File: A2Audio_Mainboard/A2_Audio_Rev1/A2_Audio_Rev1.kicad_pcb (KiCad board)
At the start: 4 copper layers, 194 x 109.5 mm, 217 parts, among them IC1 ES9822QPRO, J1 Battery_Connector, J3 BOOT_JUMPER, J4 12401610E4_2A, J5 104031-0811, J6 SFV15R-1STE1HLF, J7 SJ2-35954B-SMT-TR, SW1 SW_Wuerth_450301014042, SW10 EVQ-PUJ02K, SW11 EVQ-PUJ02K, SW4 SW_Wuerth_450301014042, SW8 EVQ-PUJ02K, SW9 EVQ-PUJ02K, U1 USBLC6-2SC6, U10 OPA1622IDRCR, U11 SI4732-A10-GS, U12 OPA1612AIDR, U13 LT3042xMSE, U14 W25Q16JVSS, U15 CM5108000, U16 AP2112K-3.3, U17 AP2112K-1.8, U18 LT6711A, U19 TPS62130, U2 TPS65987DDHRSHR, U20 AP2112K-1.8, U21 TPS61230DRC, U22 AP2112K-1.2, U23 LTC2954ITS8-1_TRPBF, U25 LT3094xDD, U26 TS5A3159DBVR, U27 TPS65131RGE, U3 TUSB546A-DCIRNQR, U4 BQ25895RTWR, U5 MAX17055ETB_T, U6 U_DAC_L, U7 U_DAC_R, U8 TPS7A2018PDBVR, U9 TPS7A2033PDBVR, Y1 Crystal, Y2 27MHz

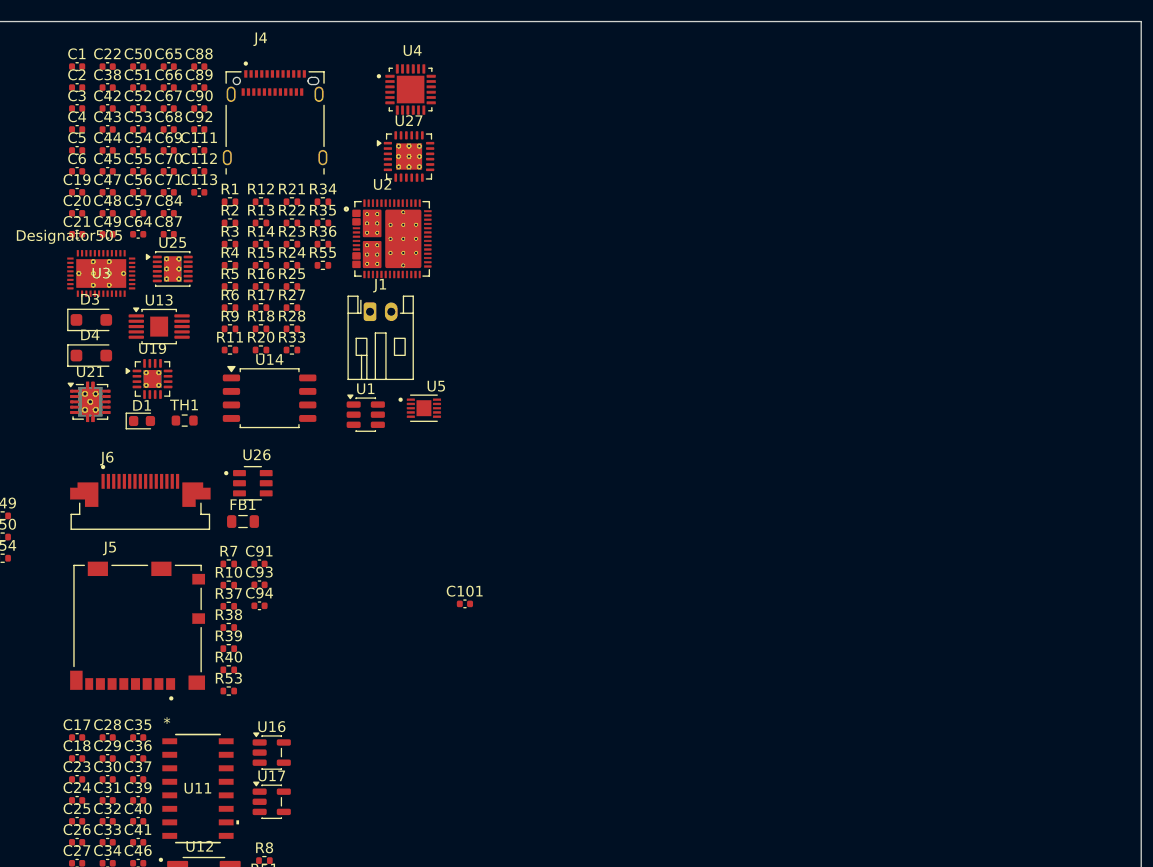
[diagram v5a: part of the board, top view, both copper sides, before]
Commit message: Fixed SD Card logic and power error
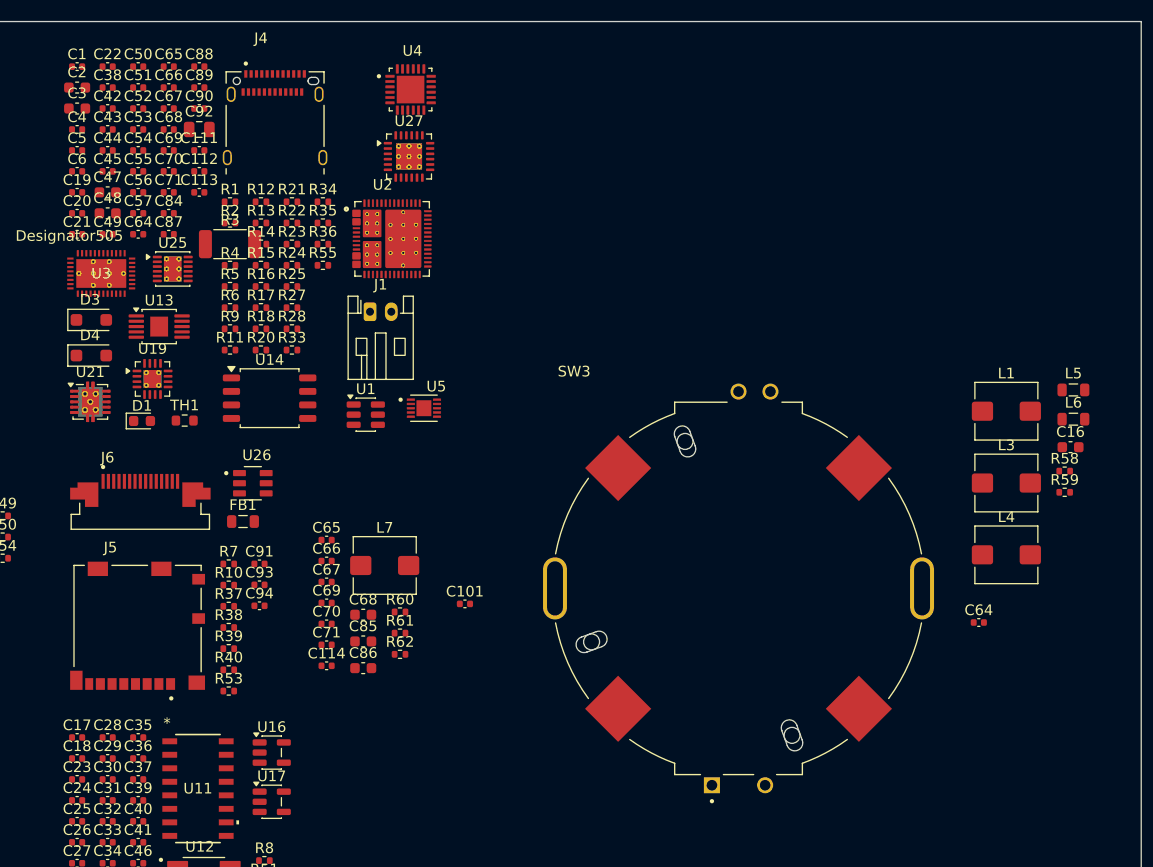
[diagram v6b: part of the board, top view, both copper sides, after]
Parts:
- added C114: 0.1µF, Capacitor_SMD:C_0402_1005Metric, F.Cu at (168.9, 107.3)
- added C16: 10µF, Capacitor_SMD:C_0603_1608Metric, F.Cu at (238.9, 86.8)
- added C64: 10µF, Capacitor_SMD:C_0402_1005Metric, F.Cu at (230.2, 103.2)
- added C65: 0.1µF, Capacitor_SMD:C_0402_1005Metric, F.Cu at (168.9, 95.5)
- added C66: 10µF, Capacitor_SMD:C_0402_1005Metric, F.Cu at (168.9, 97.5)
- added C67: 0.1µF, Capacitor_SMD:C_0402_1005Metric, F.Cu at (168.9, 99.4)
- added C68: 47nF, Capacitor_SMD:C_0603_1608Metric, F.Cu at (172.4, 102.5)
- added C69: 4.7nF, Capacitor_SMD:C_0402_1005Metric, F.Cu at (168.9, 101.4)
- added C70: 220pF, Capacitor_SMD:C_0402_1005Metric, F.Cu at (168.9, 103.4)
- added C71: 1µF, Capacitor_SMD:C_0402_1005Metric, F.Cu at (168.9, 105.3)
- added C85: 22µF, Capacitor_SMD:C_0603_1608Metric, F.Cu at (172.4, 105.0)
- added C86: 22µF, Capacitor_SMD:C_0603_1608Metric, F.Cu at (172.4, 107.5)
- added L1: 1µH, Inductor_SMD:L_Bourns_SRP5030T, F.Cu at (232.8, 83.4)
- added L3: 2.2µH, Inductor_SMD:L_Bourns_SRP5030T, F.Cu at (232.8, 90.1)
- added L4: 1.0µH, Inductor_SMD:L_Bourns_SRP5030T, F.Cu at (232.8, 96.9)
- added L5: 4.7µH, Inductor_SMD:L_0805_2012Metric, F.Cu at (239.1, 81.4)
- added L6: 4.7µH, Inductor_SMD:L_0805_2012Metric, F.Cu at (239.1, 84.1)
- added L7: 1.0µH, Inductor_SMD:L_Bourns_SRP5030T, F.Cu at (174.4, 97.9)
- added R58: 100kΩ, Resistor_SMD:R_0402_1005Metric, F.Cu at (238.3, 89.0)
- added R59: 100kΩ, Resistor_SMD:R_0402_1005Metric, F.Cu at (238.3, 91.0)
- added R60: 120kΩ, Resistor_SMD:R_0402_1005Metric, F.Cu at (175.8, 102.2)
- added R61: 15kΩ, Resistor_SMD:R_0402_1005Metric, F.Cu at (175.8, 104.2)
- added R62: 10kΩ, Resistor_SMD:R_0402_1005Metric, F.Cu at (175.8, 106.2)
- added SW3: RotaryEncoder_Switch, custom:XDCR_RING35-203010-TH, F.Cu at (207.7, 100.0)
- C2, C3, C47, C48: footprint Capacitor_SMD:C_0402_1005Metric -> Capacitor_SMD:C_0603_1608Metric
- C92: value 4.7µF -> 22µF; footprint Capacitor_SMD:C_0402_1005Metric -> Capacitor_SMD:C_0805_2012Metric
- R28: value 23.7kΩ -> 402kΩ
- R3: footprint Resistor_SMD:R_0402_1005Metric -> Resistor_SMD:R_2010_5025Metric
- R34: value 806kΩ -> 1.0MΩ
- R36: value 10kΩ -> 124kΩ
- R4, R5: value 49.9kΩ -> 45.3kΩ
- R9: value R -> 1kΩ
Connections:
- C17 pad 1: /Audio_Engine/-5V_AMP -> EXP
- C23 pad 1: Net-(IC1-AVCC) -> /Recording&Radio_Engine/3v
- C26 pad 1: Net-(IC1-CHIP_EN) -> /Recording&Radio_Engine/3v
- C27 pad 2: Net-(IC1-CHIP_EN) -> /Recording&Radio_Engine/3v
- C28 pad 2: Net-(IC1-AVCC) -> /Recording&Radio_Engine/+5V_AMP
- C29 pad 2: Net-(IC1-AVCC) -> /Recording&Radio_Engine/+5V_AMP
- C30 pad 2: Net-(IC1-AVCC) -> /Recording&Radio_Engine/3v
- C31 pad 2: Net-(IC1-AVCC) -> /Recording&Radio_Engine/+5V_AMP
- C41 pad 1: Net-(IC1-AVCC) -> /Recording&Radio_Engine/3v
- C46 pad 1: Net-(IC1-CHIP_EN) -> Net-(U17-VOUT)
- C80 pad 1: /Power&Battery/DP_AUX_P -> /Power&Battery/DP_AUX_N
- C81 pad 1: /Power&Battery/DP_AUX_N -> /Power&Battery/DP_AUX_P
- C92 pad 2: /Audio_Engine/-5V_AMP -> EXP
- IC1 pad 10: Net-(IC1-AVCC) -> /Recording&Radio_Engine/+5V_AMP
- IC1 pad 21: Net-(IC1-AVCC) -> /Recording&Radio_Engine/+5V_AMP
- IC1 pad 23: Net-(IC1-CHIP_EN) -> /Recording&Radio_Engine/3v
- IC1 pad 29: Net-(IC1-CHIP_EN) -> Net-(IC1-DVDD)
- IC1 pad 30: Net-(IC1-AVCC) -> /Recording&Radio_Engine/3v
- IC1 pad 5: Net-(IC1-AVCC) -> /Recording&Radio_Engine/+5V_AMP
- R21 pad 2: /+3V3_SYS -> CM5_3.3V(OUTPUT)
- R22 pad 2: /+3V3_SYS -> CM5_3.3V(OUTPUT)
- R25 pad 2: /+3V3_SYS -> CM5_3.3V(OUTPUT)
- R29 pad 1: /+3V3_SYS -> CM5_3.3V(OUTPUT)
- R30 pad 1: /+3V3_SYS -> CM5_3.3V(OUTPUT)
- R41 pad 2: /+3V3_SYS -> CM5_3.3V(OUTPUT)
- R42 pad 1: /+3V3_SYS -> CM5_3.3V(OUTPUT)
- R43 pad 2: /+3V3_SYS -> CM5_3.3V(OUTPUT)
- R44 pad 1: /+3V3_SYS -> CM5_3.3V(OUTPUT)
- R45 pad 1: /+3V3_SYS -> CM5_3.3V(OUTPUT)
- R46 pad 1: /+3V3_SYS -> CM5_3.3V(OUTPUT)
- R47 pad 1: /+3V3_SYS -> CM5_3.3V(OUTPUT)
- R48 pad 1: /+3V3_SYS -> CM5_3.3V(OUTPUT)
- R49 pad 1: /+3V3_SYS -> CM5_3.3V(OUTPUT)
- R53 pad 2: /+3V3_SYS -> CM5_3.3V(OUTPUT)
- R54 pad 2: /+3V3_SYS -> CM5_3.3V(OUTPUT)
- R6 pad 2: /+3V3_SYS -> CM5_3.3V(OUTPUT)
- R8 pad 2: Net-(IC1-AVCC) -> /Recording&Radio_Engine/3v
- U10 pad 11: GND -> EXP
- U10 pad 12: GND -> EXP
- U10 pad 13: GND -> EXP
- U10 pad 14: GND -> EXP
- U10 pad 15: GND -> EXP
- U10 pad 4: /Audio_Engine/-5V_AMP -> EXP
- U11 pad 14: Net-(IC1-AVCC) -> /Recording&Radio_Engine/3v
- U12 pad 4: /Audio_Engine/-5V_AMP -> EXP
- U14 pad 3: /+3V3_SYS -> Net-(U14-VCC)
- U15 pad 75: unconnected-(U15A-SD_PWR_ON-Pad75) -> /VDD_OVERRIDE
- U15 pad 78: unconnected-(U15A-GPIO_VREF-Pad78) -> CM5_3.3V(OUTPUT)
- U16 pad 5: Net-(IC1-AVCC) -> /Recording&Radio_Engine/3v
- U17 pad 5: Net-(IC1-CHIP_EN) -> Net-(U17-VOUT)
- U25 pad 10: /Audio_Engine/-5V_AMP -> EXP
- U25 pad 11: /Audio_Engine/-5V_AMP -> EXP
- U25 pad 12: /Audio_Engine/-5V_AMP -> EXP
- U6 pad 25: /Audio_Engine/3V3_ANA -> /Audio_Engine/1V8_DIG
- U6 pad 31: /Audio_Engine/3V3_ANA -> /Audio_Engine/1V8_DIG
- U6 pad 7: /Audio_Engine/3V3_ANA -> /Audio_Engine/1V8_DIG
- U7 pad 25: /Audio_Engine/3V3_ANA -> /Audio_Engine/1V8_DIG
- U7 pad 30: /Audio_Engine/3V3_ANA -> /Audio_Engine/1V8_DIG
- U7 pad 31: /Audio_Engine/3V3_ANA -> /Audio_Engine/1V8_DIG
- U7 pad 7: /Audio_Engine/3V3_ANA -> /Audio_Engine/1V8_DIG
